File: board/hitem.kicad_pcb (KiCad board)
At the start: 2 copper layers, 70 x 44 mm, 65 parts, among them J1 Male, 0.1", 2x4, J2 Male, 0.1", 1x2, J3 Female, 0.1", 2x5, J4 Male, 0.1", 2x2, J5 Female, 0.1", 1x10, J6 Female, 0.1", 1x10, Q1 BSS214N, Q2 BSS214N, Q3 BSS214N, Q4 BSS214N, Q5 BSS214N, Q6 BSS214N, U1 TPS61070, U2 LIS2HH12TR

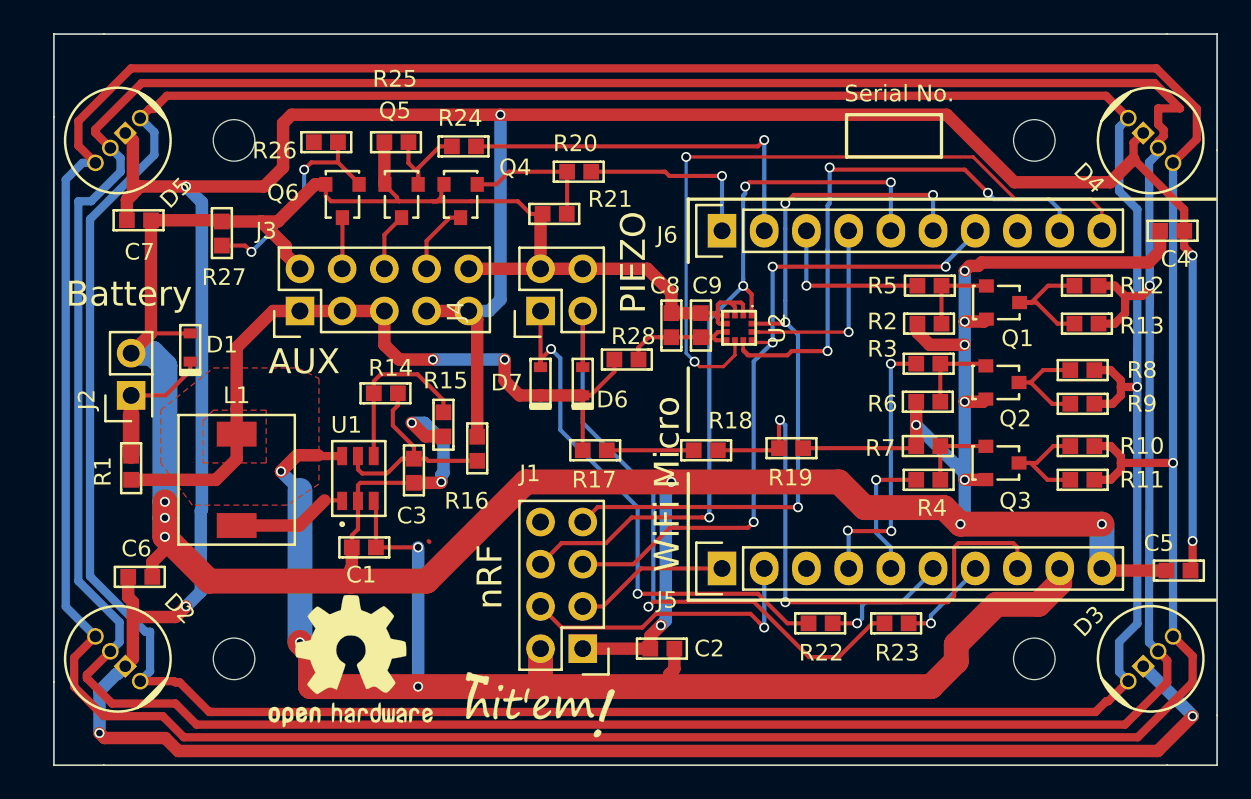
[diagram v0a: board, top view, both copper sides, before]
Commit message: Finish schematic & board layout (without routing)
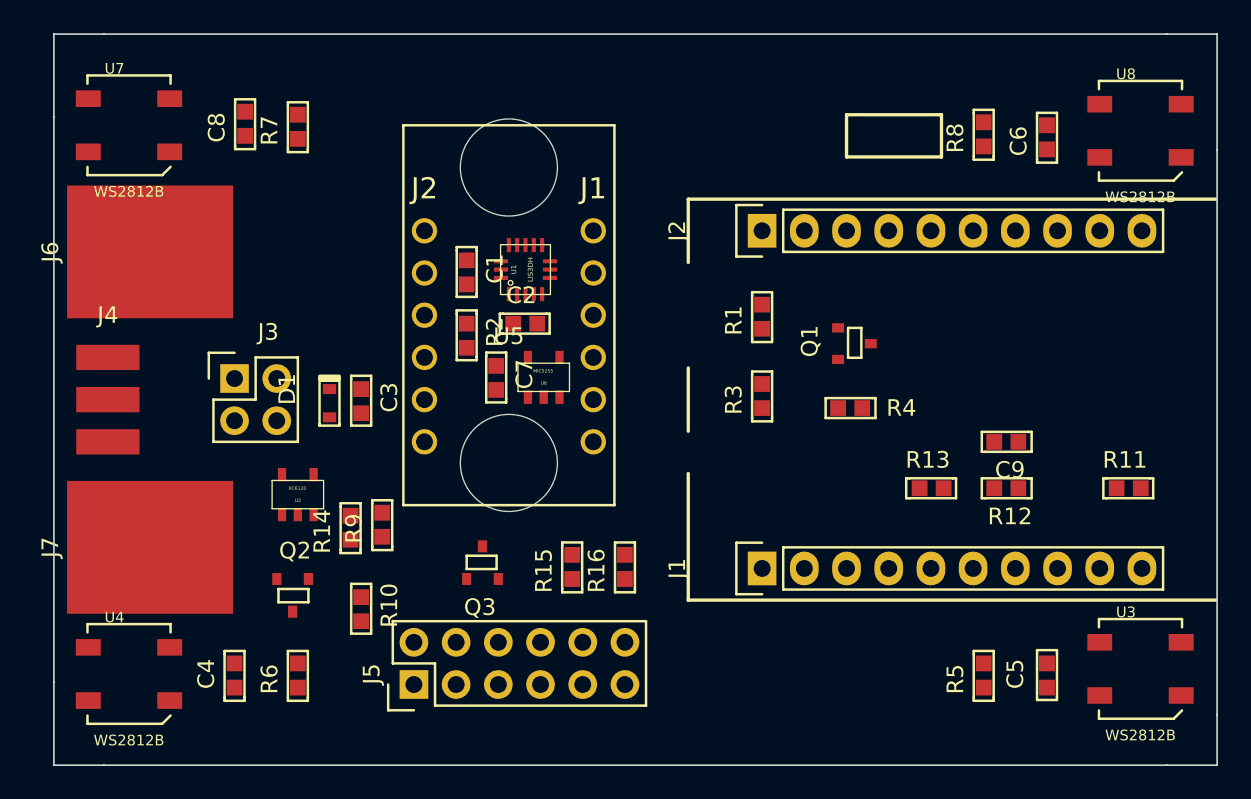
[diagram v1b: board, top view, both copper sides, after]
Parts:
- removed D2, D3, D4, D5: LED_RABG, avishay:LED_RGB_TH_5MM
- removed D6, D7: CDBU0130L, avishay:SOD-523F
- removed G***: LOGO, board:hitem
- removed G***: LOGO, board:oshw
- removed L1: B82462G4472M, avishay:B82462G4472M
- removed Q4, Q5, Q6: BSS214N, avishay:BSS214NH6327
- removed R17, R18, R19: 180K, avishay:R0603
- removed R20, R24, R26: 1K, avishay:R0603
- removed R21, R25, R27: 1.6M, avishay:R0603
- removed R22, R23: 100K, avishay:R0603
- removed R28: 0, avishay:R0603
- removed REF** (x4): MountingHole_2-5mm, Mounting_Holes:MountingHole_2-5mm
- added J7: CONN_01X01, hitem:BATTERY_CONTACT, F.Cu at (157.5, 63.5)
- added U3: WS2812B, hitem:WS2812, F.Cu at (217.1, 70.8)
- added U4: WS2812B, hitem:WS2812, F.Cu at (156.2, 71.1)
- added U5: SPARKFUN_LIS3DH, avishay:SEN-13963, F.Cu at (172.7, 38.1)
- added U6: MIC5255, hitem:MIC5255, F.Cu at (181.2, 53.3)
- added U7: WS2812B, hitem:WS2812, F.Cu at (156.2, 38.1)
- added U8: WS2812B, hitem:WS2812, F.Cu at (217.1, 38.4)
- C1, C3: value 10uF -> 1uF
- C2: value 1uF -> 0.1u
- C7: value 1uF -> 0.01uF
- C8, C9: value 0.1u -> 1uF
- J1: value Male, 0.1", 2x4 -> Female, 0.1", 1x10; footprint Pin_Headers:Pin_Header_Straight_2x04 -> Pin_Headers:Pin_Header_Straight_1x10
- J2: value Male, 0.1", 1x2 -> Female, 0.1", 1x10; footprint Pin_Headers:Pin_Header_Straight_2x01 -> Pin_Headers:Pin_Header_Straight_1x10
- J3: value Female, 0.1", 2x5 -> Header, .100"; footprint Pin_Headers:Pin_Header_Straight_2x05 -> Pin_Headers:Pin_Header_Straight_2x02
- J4: value Male, 0.1", 2x2 -> CONN_01X03; footprint Pin_Headers:Pin_Header_Straight_2x02 -> avishay:SMT_HOOKUP_3
- J5: value Female, 0.1", 1x10 -> Header, .100"; footprint Pin_Headers:Pin_Header_Straight_1x10 -> Pin_Headers:Pin_Header_Straight_2x06
- J6: value Female, 0.1", 1x10 -> CONN_01X01; footprint Pin_Headers:Pin_Header_Straight_1x10 -> hitem:BATTERY_CONTACT
- Q1, Q2, Q3: footprint avishay:BSS214NH6327 -> avishay:SOT-23
- R1: value 0 -> 1K
- R10, R11, R12, R13: value 50 -> 180K
- R14: value 1.6M -> 1K
- R15: value 180K -> 1K
- R16: value 0 -> 1.6M
- R2: value 1K -> 0
- R3: value 1K -> 1.6M
- R4: value 1K -> 47K
- R5, R6, R7: value 1.6M -> 0
- R8, R9: value 50 -> 0
- U1: value TPS61070 -> LIS3DH; footprint avishay:TPS61070DDCR -> hitem:LIS3DH
- U2: value LIS2HH12TR -> XC6120; footprint avishay:LIS2HH12 -> hitem:XC6221
- moved C4 63.4 mm to (162.6, 71.9), turned to 90 degrees
- moved C6 61.0 mm to (211.5, 39.5), turned to 90 degrees
- moved R10 45.0 mm to (170.2, 66.5), turned to 270 degrees
- moved R9 43.6 mm to (171.4, 62.9), turned to 90 degrees
- moved Q2 42.7 mm to (167.0, 65.4), turned to 180 degrees
- moved R7 41.6 mm to (166.4, 38.9), turned to 90 degrees
- moved R6 41.0 mm to (166.4, 71.9), turned to 90 degrees
- moved J2 39.2 mm to (194.3, 44.5)
- moved R1 39.0 mm to (194.3, 50.3)
- moved J6 34.4 mm to (157.5, 45.7)
- moved Q3 32.2 mm to (176.5, 65.4), turned to 0 degrees
- moved R2 28.7 mm to (176.5, 50.0), turned to 270 degrees
- moved U2 28.4 mm to (166.4, 60.3), turned to 0 degrees
- moved C8 28.4 mm to (163.2, 38.7)
- moved J4 27.2 mm to (154.9, 57.1), turned to 0 degrees
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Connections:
- net /NRF_INT renamed Net-(J1-Pad8)
- C1 pad 1: +BATT -> Net-(C1-Pad1)
- C2 pad 1: GND -> Net-(C1-Pad1)
- C2 pad 2: +BATT -> GND
- C3 pad 1: Net-(C3-Pad1) -> +BATT
- C3 pad 2: GND -> Net-(C3-Pad2)
- C4 pad 1: +5V -> +BATT
- C5 pad 1: +5V -> +BATT
- C6 pad 1: +5V -> +BATT
- C7 pad 1: +5V -> Net-(C7-Pad1)
- C8 pad 1: Net-(R28-Pad1) -> +BATT
- C9 pad 1: Net-(R28-Pad1) -> /VSENSE
- D1 pad 1: Net-(D1-Pad1) -> +BATT
- D1 pad 2: GND -> Net-(C3-Pad2)
- J1 pad 1: GND -> /AUX1
- J1 pad 2: +BATT -> /AUX2
- J1 pad 3: /NRF_CE -> /RX1
- J1 pad 4: /NRF_CS -> /TX1
- J1 pad 5: /SPI_SCK -> Net-(J1-Pad5)
- J1 pad 6: /SPI_MOSI -> /ACCEL_INT
- J1 pad 7: /SPI_MISO -> /VSENSE
- J2 pad 1: Net-(D1-Pad1) -> /LED
- J2 pad 2: GND -> /AUX3
- J3 pad 1: +BATT -> Net-(J3-Pad1)
- J3 pad 2: GND -> +BATT
- J3 pad 3: +BATT -> Net-(J3-Pad3)
- J3 pad 4: Net-(J3-Pad4) -> Net-(C3-Pad2)
- J4 pad 1: Net-(D7-Pad2) -> +BATT
- J4 pad 2: GND -> Net-(J4-Pad2)
- J4 pad 3: Net-(D6-Pad2) -> GND
- J5 pad 1: /NRF_CE -> GND
- J5 pad 10: GND -> /TX1
- J5 pad 2: /NRF_CS -> +BATT
- J5 pad 4: /LED1 -> +BATT
- J5 pad 5: /LED2 -> GND
- J5 pad 6: /PIEZO1 -> +3V3
- J5 pad 7: /PIEZO2 -> /AUX3
- J5 pad 8: /VSENSE -> /AUX1
- J5 pad 9: +BATT -> /AUX2
- J6 pad 1: /LD1 -> Net-(J3-Pad1)
- Q2 pad 2: GND -> Net-(C3-Pad2)
- Q2 pad 3: Net-(Q2-Pad3) -> GND
- Q3 pad 3: Net-(Q3-Pad3) -> Net-(J5-Pad3)
- R1 pad 1: +BATT -> Net-(Q1-Pad1)
- R1 pad 2: Net-(D1-Pad1) -> /LED
- R10 pad 1: Net-(D2-Pad4) -> Net-(Q2-Pad1)
- R10 pad 2: Net-(Q3-Pad3) -> +BATT
- R11 pad 1: Net-(D2-Pad4) -> Net-(R11-Pad1)
- R11 pad 2: Net-(Q3-Pad3) -> +BATT
- R12 pad 1: Net-(D2-Pad3) -> /VSENSE
- R12 pad 2: Net-(Q1-Pad3) -> Net-(R11-Pad1)
- R13 pad 1: Net-(D2-Pad3) -> GND
- R13 pad 2: Net-(Q1-Pad3) -> /VSENSE
- R14 pad 1: Net-(R14-Pad1) -> Net-(Q2-Pad1)
- R14 pad 2: Net-(C3-Pad1) -> Net-(R14-Pad2)
- R15 pad 1: GND -> Net-(Q3-Pad1)
- R15 pad 2: Net-(R14-Pad1) -> /LD1
- R16 pad 1: +5V -> GND
- R16 pad 2: Net-(C3-Pad1) -> Net-(Q3-Pad1)
- R2 pad 1: Net-(Q1-Pad1) -> Net-(C1-Pad1)
- R2 pad 2: /LED3 -> +3V3
- R3 pad 1: Net-(Q2-Pad1) -> GND
- R3 pad 2: /LED1 -> Net-(Q1-Pad1)
- R4 pad 1: Net-(Q3-Pad1) -> Net-(Q1-Pad3)
- R4 pad 2: /LED2 -> +BATT
- R5 pad 1: GND -> Net-(R5-Pad1)
- R5 pad 2: Net-(Q1-Pad1) -> Net-(Q1-Pad3)
- R6 pad 1: GND -> Net-(R6-Pad1)
- R6 pad 2: Net-(Q2-Pad1) -> Net-(R5-Pad1)
- R7 pad 1: GND -> Net-(R7-Pad1)
- R7 pad 2: Net-(Q3-Pad1) -> Net-(R6-Pad1)
- R8 pad 1: Net-(D2-Pad1) -> Net-(J4-Pad2)
- R8 pad 2: Net-(Q2-Pad3) -> Net-(R7-Pad1)
- R9 pad 1: Net-(D2-Pad1) -> GND
- R9 pad 2: Net-(Q2-Pad3) -> Net-(C3-Pad2)
- U1 pad 1: Net-(L1-Pad2) -> Net-(C1-Pad1)
- U1 pad 2: GND -> (no net)
- U1 pad 3: +BATT -> (no net)
- U1 pad 4: Net-(R14-Pad1) -> /SPI_SCK
- U1 pad 5: Net-(C3-Pad1) -> GND
- U1 pad 6: +BATT -> /SPI_MOSI
- U2 pad 1: /SPI_SCK -> (no net)
- U2 pad 2: /ACCEL_CS -> Net-(C3-Pad2)
- U2 pad 3: /SPI_MISO -> Net-(R14-Pad2)
- U2 pad 4: /SPI_MOSI -> +BATT
- U2 pad 5: GND -> (no net)
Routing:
- net GND: track 241.5 -> 0.00 mm, vias 15 -> 0
- net +5V: track 235.1 -> 0.00 mm, vias 7 -> 0
- net Net-(D2-Pad4): track 219.7 -> 0.00 mm, vias 1 -> 0
- net Net-(D2-Pad3): track 214.9 -> 0.00 mm, vias 1 -> 0
- net Net-(D2-Pad1): track 200.4 -> 0.00 mm, vias 1 -> 0
- net +BATT: track 134.4 -> 0.00 mm, vias 6 -> 0
- net /SPI_MOSI: track 45.9 -> 0.00 mm, vias 4 -> 0
- net /SPI_MISO: track 45.3 -> 0.00 mm, vias 4 -> 0
- net /ACCEL_INT2: track 43.8 -> 0.00 mm, vias 2 -> 0
- net /SPI_SCK: track 41.8 -> 0.00 mm, vias 4 -> 0
- net Net-(D6-Pad2): track 39.6 -> 0.00 mm, vias 1 -> 0
- net /VSENSE: track 35.2 -> 0.00 mm, vias 2 -> 0
- net /ACCEL_INT1: track 33.7 -> 0.00 mm, vias 3 -> 0
- net Net-(D7-Pad2): track 32.6 -> 0.00 mm, vias 2 -> 0
- net /LD2: track 23.0 -> 0.00 mm, vias 1 -> 0
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- removed copper zone on F.Cu, net +BATT
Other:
- board text removed: "AUX"
- board text removed: "Battery"
- board text removed: "PIEZO"
- board text removed: "Serial No."
- board text removed: "WiFi Micro"
- board text removed: "nRF"

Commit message: Finish PCB of REV. 2
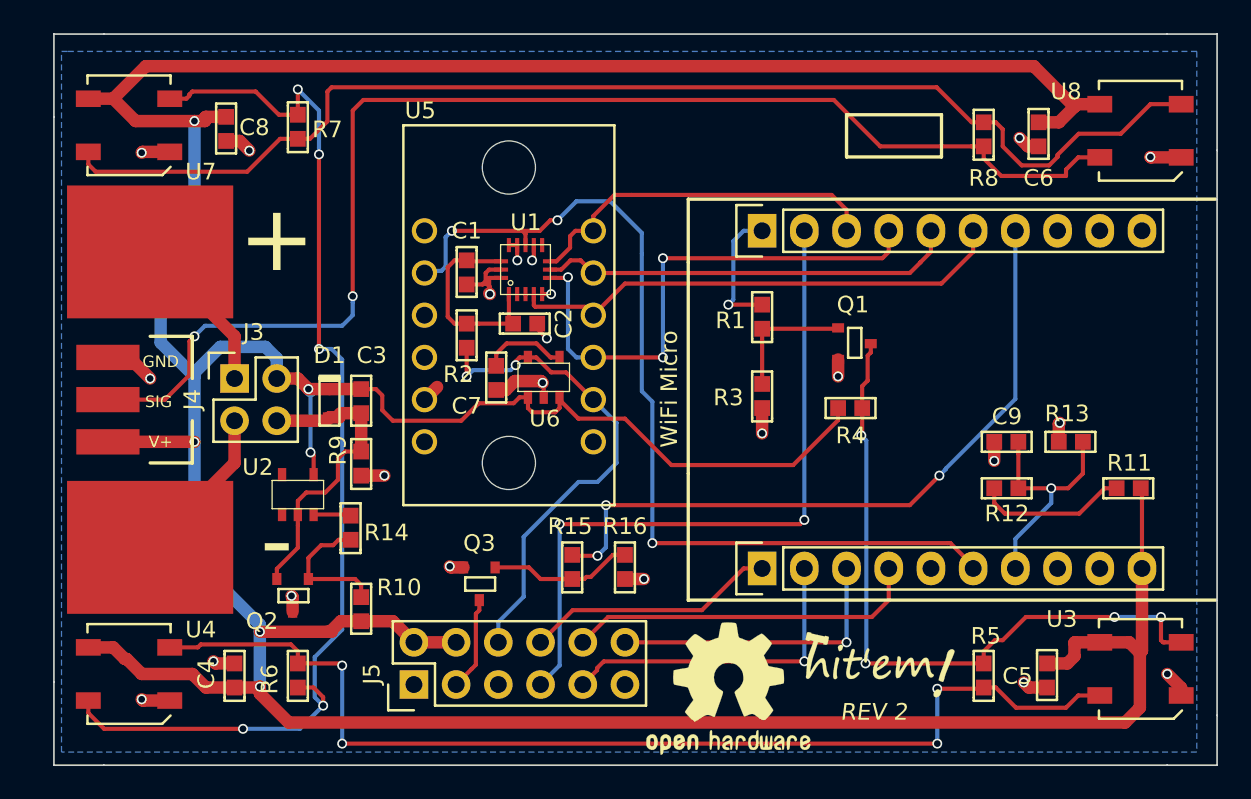
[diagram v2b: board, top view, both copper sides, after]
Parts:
- added G***: LOGO, hitem:hitem, F.Cu at (201.4, 70.6)
- added G***: LOGO, hitem:oshw, F.Cu at (192.3, 72.1)
- moved R13 8.84 mm to (212.2, 57.1)
- moved R9 3.90 mm to (170.2, 59.2)
- moved Q3 1.85 mm to (178.2, 64.7), turned to 180 degrees
- moved C6 1.71 mm to (210.9, 37.9), turned to 270 degrees
- moved C8 1.62 mm to (162.1, 37.6), turned to 270 degrees
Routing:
- net +BATT: track 0.00 -> 268.0 mm, vias 0 -> 6
- net Net-(J4-Pad2): track 0.00 -> 78.6 mm, vias 0 -> 2
- net Net-(R7-Pad1): track 0.00 -> 74.0 mm
- net Net-(R6-Pad1): track 0.00 -> 67.7 mm, vias 0 -> 5
- net Net-(R5-Pad1): track 0.00 -> 65.8 mm, vias 0 -> 4
- net /ACCEL_INT: track 0.00 -> 56.6 mm, vias 0 -> 3
- net /AUX3: track 0.00 -> 42.4 mm, vias 0 -> 2
- net /LD1: track 0.00 -> 42.2 mm, vias 0 -> 3
- net Net-(Q1-Pad3): track 0.00 -> 41.7 mm, vias 0 -> 4
- net GND: track 0.00 -> 39.8 mm, vias 0 -> 23
- net /SPI_MOSI: track 0.00 -> 32.3 mm, vias 0 -> 3
- net /SPI_SCK: track 0.00 -> 30.2 mm
- net +3V3: track 0.00 -> 29.9 mm, vias 0 -> 2
- net /SPI_MISO: track 0.00 -> 25.3 mm
- net /ACCEL_CS: track 0.00 -> 22.1 mm
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- added copper zone on B.Cu, net GND
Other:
- board text added: "+"
- board text added: "-"
- board text added: "GND"
- board text added: "REV 2"
- board text added: "SIG"
- board text added: "V+"
- board text added: "WiFi Micro"

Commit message: Fix incorrect footprint for U2
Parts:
- U2: footprint hitem:XC6221 -> hitem:SSOT-24
- moved U2 0.40 mm to (166.0, 60.3)
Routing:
- net Net-(R14-Pad2): track 2.25 -> 4.22 mm
- net +BATT: track 268.0 -> 269.5 mm
- net Net-(C3-Pad2): track 18.7 -> 19.8 mm

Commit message: Add protection Polyfuse
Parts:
- added R17: PTC, 1.5A, hitem:BEL-0ZCK, F.Cu at (164.4, 48.8)
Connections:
- J6 pad 1: Net-(J3-Pad1) -> Net-(J6-Pad1)
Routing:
- net Net-(J6-Pad1): track 0.00 -> 7.70 mm
- net Net-(J3-Pad1): track 9.72 -> 4.37 mm
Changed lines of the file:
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@@
 (kicad_pcb (version 4) (host pcbnew 4.0.3-1.fc24-product)
   (general
-    (links 113)
-    (no_connects 4)
-    (area 148.505 32.559999 239.422671 85.130271)
+    (links 114)
+    (no_connects 2)
+    (area 151.639999 32.559999 221.740001 76.660001)
     (thickness 1.6)
     (drawings 37)
-    (tracks 523)
+    (tracks 527)
     (zones 0)
-    (modules 46)
-    (nets 40)
+    (modules 47)
+    (nets 41)
   )
   (page A4)
@@
   (net 38 "Net-(U5-Pad12)")
   (net 39 "Net-(U1-Pad9)")
+  (net 40 "Net-(J6-Pad1)")
   (net_class Default "This is the default net class."
     (clearance 0.16)
@@
     (add_net "Net-(J4-Pad2)")
     (add_net "Net-(J5-Pad3)")
+    (add_net "Net-(J6-Pad1)")
     (add_net "Net-(Q1-Pad1)")
     (add_net "Net-(Q1-Pad3)")
@@
     )
     (pad 1 smd rect (at 0 0 180) (size 10 8) (layers F.Cu F.Mask)
-      (net 36 "Net-(J3-Pad1)"))
+      (net 40 "Net-(J6-Pad1)"))
   )
   (module hitem:BATTERY_CONTACT (layer F.Cu)
@@
     (descr "Through hole pin header")
     (tags "pin header")
-    (fp_text reference J3 (at 1.143 -2.794) (layer F.SilkS)
+    (fp_text reference J3 (at -0.99 -2.46) (layer F.SilkS)
       (effects (font (size 1 1) (thickness 0.15)))
     )
@@
       (net 1 +BATT))
   )
+  (module hitem:BEL-0ZCK (layer F.Cu)
+    (at 164.37 48.78 90)
+    (fp_text reference R17 (at 1.7 3.1 180) (layer F.SilkS)
+      (effects (font (size 1 1) (thickness 0.15)))
+    )
+    (fp_text value "PTC, 1.5A" (at 0 -2.5 90) (layer F.Fab)
+      (effects (font (size 1 1) (thickness 0.15)))
+    )
+    (fp_line (start 2.25 1.5) (end 1.25 1.5) (layer F.SilkS) (width 0.15))
+    (fp_line (start 2.25 -1.5) (end 2.25 1.5) (layer F.SilkS) (width 0.15))
+    (fp_line (start 1.25 -1.5) (end 2.25 -1.5) (layer F.SilkS) (width 0.15))
+    (fp_line (start -2.25 1.5) (end -1.25 1.5) (layer F.SilkS) (width 0.15))
+    (fp_line (start -2.25 -1.5) (end -2.25 1.5) (layer F.SilkS) (width 0.15))
+    (fp_line (start -1.25 -1.5) (end -2.25 -1.5) (layer F.SilkS) (width 0.15))
+    (pad 1 smd rect (at -1.1 0 90) (size 1 1.5) (layers F.Cu F.Paste F.Mask)
+      (net 36 "Net-(J3-Pad1)"))
+    (pad 2 smd rect (at 1.1 0 90) (size 1 1.5) (layers F.Cu F.Paste F.Mask)
+      (net 40 "Net-(J6-Pad1)"))
+  )
   (dimension 44.000114 (width 0.3) (layer Dwgs.User)
     (gr_text "44.000 mm" (at 232.922671 54.605688 89.86978254) (layer Dwgs.User)
@@
     (effects (font (size 4 4) (thickness 1)))
   )
-  (gr_text + (at 165.1 44.958) (layer F.SilkS)
+  (gr_text + (at 165.1 43.08) (layer F.SilkS)
     (effects (font (size 4 4) (thickness 1)))
   )
@@
   (segment (start 167.12 59.4) (end 168.17 60.45) (width 0.25) (layer F.Cu) (net 35))
   (segment (start 169.47388 61.52388) (end 169.545 61.595) (width 0.25) (layer F.Cu) (net 35))
-  (segment (start 162.56 53.34) (end 162.56 50.8) (width 1.5) (layer F.Cu) (net 36))
-  (segment (start 162.56 50.8) (end 157.48 45.72) (width 1.5) (layer F.Cu) (net 36))
+  (segment (start 164.37 49.88) (end 162.56 51.69) (width 1.5) (layer F.Cu) (net 36))
+  (segment (start 162.56 51.69) (end 162.56 53.34) (width 1.5) (layer F.Cu) (net 36))
+  (segment (start 164.37 49.98) (end 164.3064 49.98) (width 0.75) (layer F.Cu) (net 36))
+  (segment (start 164.37 49.88) (end 164.37 49.98) (width 0.75) (layer F.Cu) (net 36))
   (segment (start 162.56 55.88) (end 162.56 58.42) (width 1.5) (layer F.Cu) (net 37))
   (segment (start 162.56 58.42) (end 157.48 63.5) (width 1.5) (layer F.Cu) (net 37))
+  (segment (start 164.37 47.68) (end 159.44 47.68) (width 1.5) (layer F.Cu) (net 40))
+  (segment (start 159.44 47.68) (end 157.48 45.72) (width 1.5) (layer F.Cu) (net 40))
   (zone (net 2) (net_name GND) (layer B.Cu) (hatch edge 0.508)
     (connect_pads (clearance 0.508))
